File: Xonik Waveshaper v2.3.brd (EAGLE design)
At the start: 55.9 x 21 mm, 78 parts, among them IC1 TL074JT, IC2 TL074JT, IC3 TL074JT, IC4 TL072JT, IC5 4013T, IC6 LM311D, T1 2n3904

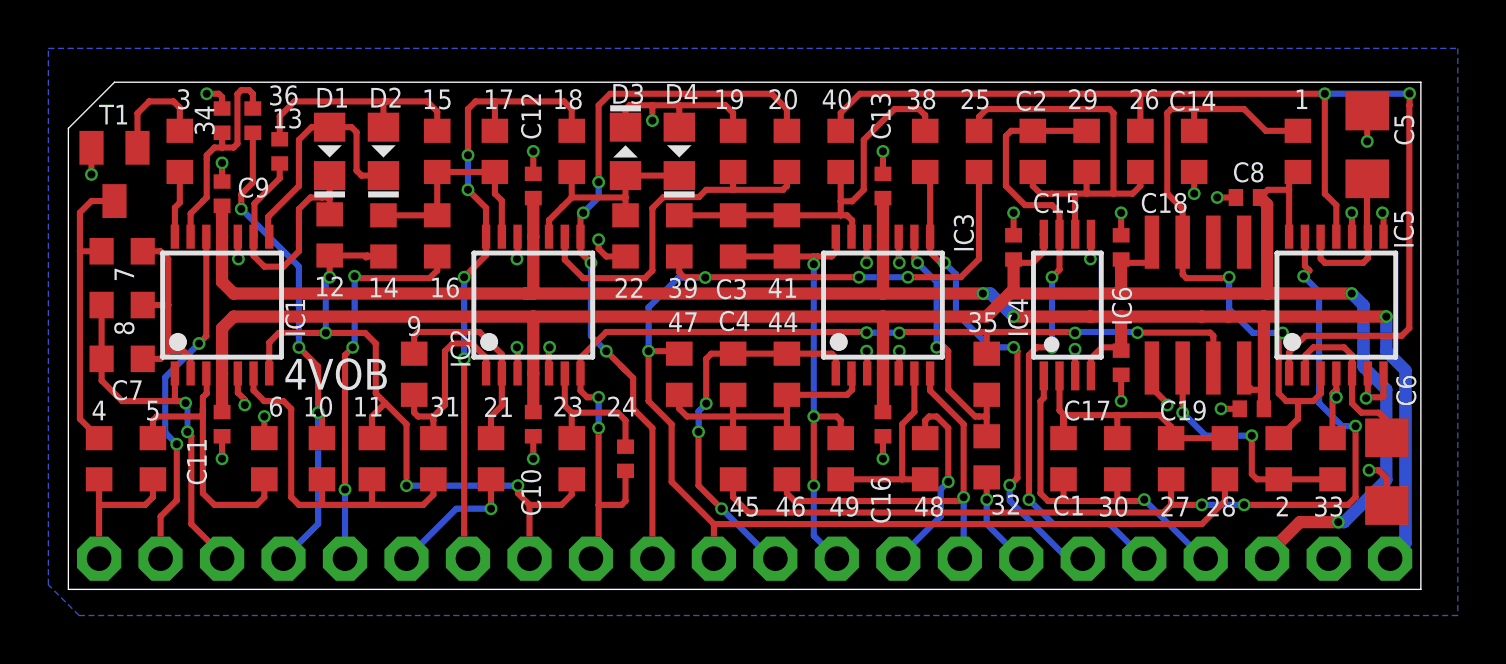
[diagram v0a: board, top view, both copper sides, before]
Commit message: Replaced LM311 with op amp comparator
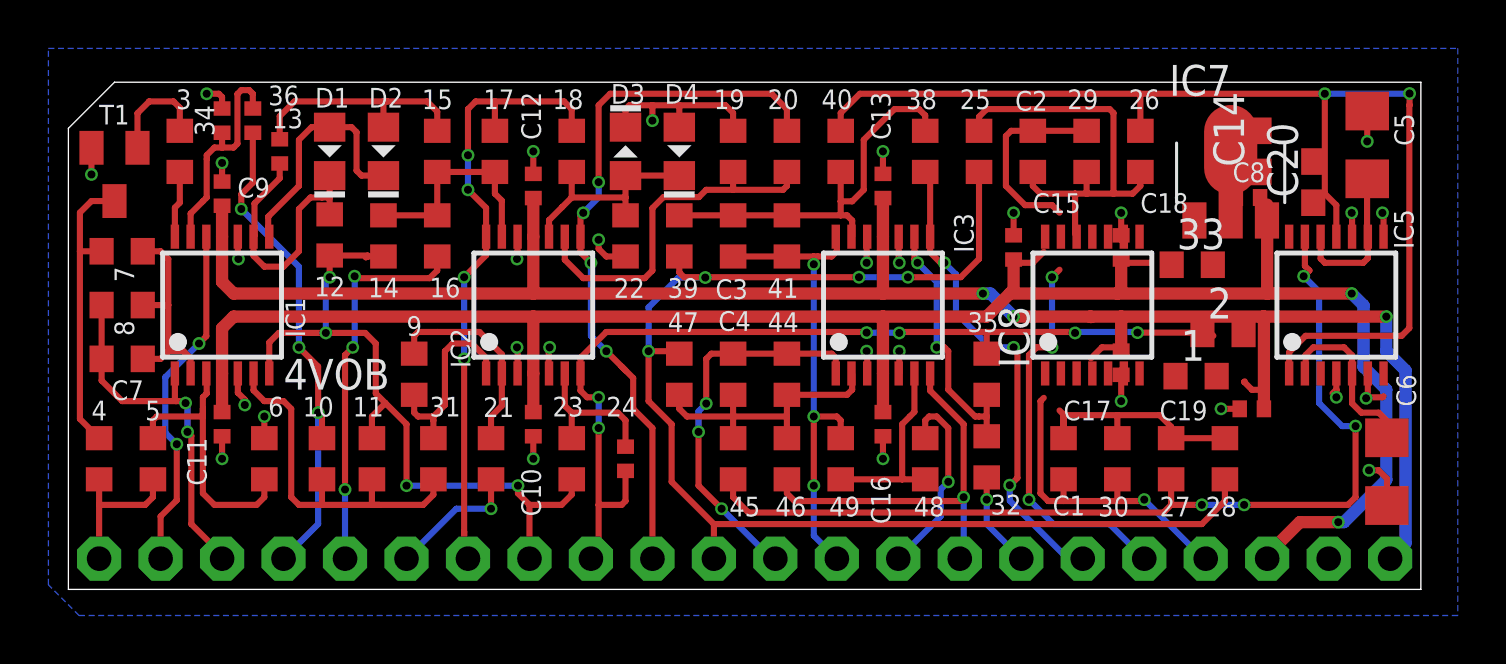
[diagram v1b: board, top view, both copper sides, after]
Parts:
- removed IC4: TL072JT, joakim:TSSOP8J
- removed IC6: LM311D, joakim:SO08J
- added C20: 0.33uF, resistor:C0603
- added IC7: 78L05F, linear:SOT89
- added IC8: TL074JT, joakim:TSSOP14J
- 1: value 510R -> 100k
- 26, 27: value 24k -> 10k
- 33: value 1k -> 20k
- 40, 45: value 120k -> 50k
- C14: value 820pF -> 0.1uF; device joakim:C0603-J -> resistor:C0603
- moved 1 10.2 mm to (46.6, 8.81), turned to 0 degrees
- moved 33 9.89 mm to (46.4, 13.4), turned to 0 degrees
- moved 2 5.65 mm to (47.7, 10.6), turned to 0 degrees
- moved C14 2.70 mm to (49.2, 18.1)
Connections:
- removed net N$25: 2.2, 33.1, IC6.2
- removed net SQR: 1.1, 2.1, C14.2, IC5.3, IC6.7
- new net +5V: C14.2, C8.2, IC5.14, IC7.1
- new net N$17: 33.2, IC5.3, IC8.8
- new net N$7: 1.1, IC8.7
- new net N$9: 1.2, 2.2, 33.1, IC8.9
- net +12V: now also C20.2, IC7.3, IC8.4; no longer 1.2, C8.2, IC4.8, IC5.14, IC6.8
- net -12V: now also 2.1, IC8.11; no longer IC4.4, IC6.4
- net GND: now also C20.1, IC7.2, IC7.2@1, IC8.10, IC8.12, IC8.3, IC8.6; no longer 33.2, IC4.3, IC4.5, IC6.1
- net N$19: now also IC8.13; no longer IC4.6
- net N$22: now also IC8.2; no longer IC4.2
- net SAW: now also IC8.5; no longer IC6.3
- net SUB_SQR_1: now also IC8.14; no longer IC4.7
- net SUB_SQR_2: now also IC8.1; no longer IC4.1
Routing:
- net SQR: track 27.1 -> 0.00 mm, vias 2 -> 0
- net N$25: track 10.2 -> 0.00 mm, vias 2 -> 0
- net GND: track 48.0 -> 39.6 mm, vias 35 -> 30
- net +12V: track 89.1 -> 82.8 mm
- net SUB_SQR_1: track 26.7 -> 24.4 mm
- net -12V: track 81.2 -> 79.5 mm
- net N$22: track 12.0 -> 10.5 mm
- net SAW: track 40.4 -> 39.1 mm
- net SUB_SQR_2: track 15.0 -> 13.9 mm

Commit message: Routed new version of comparator
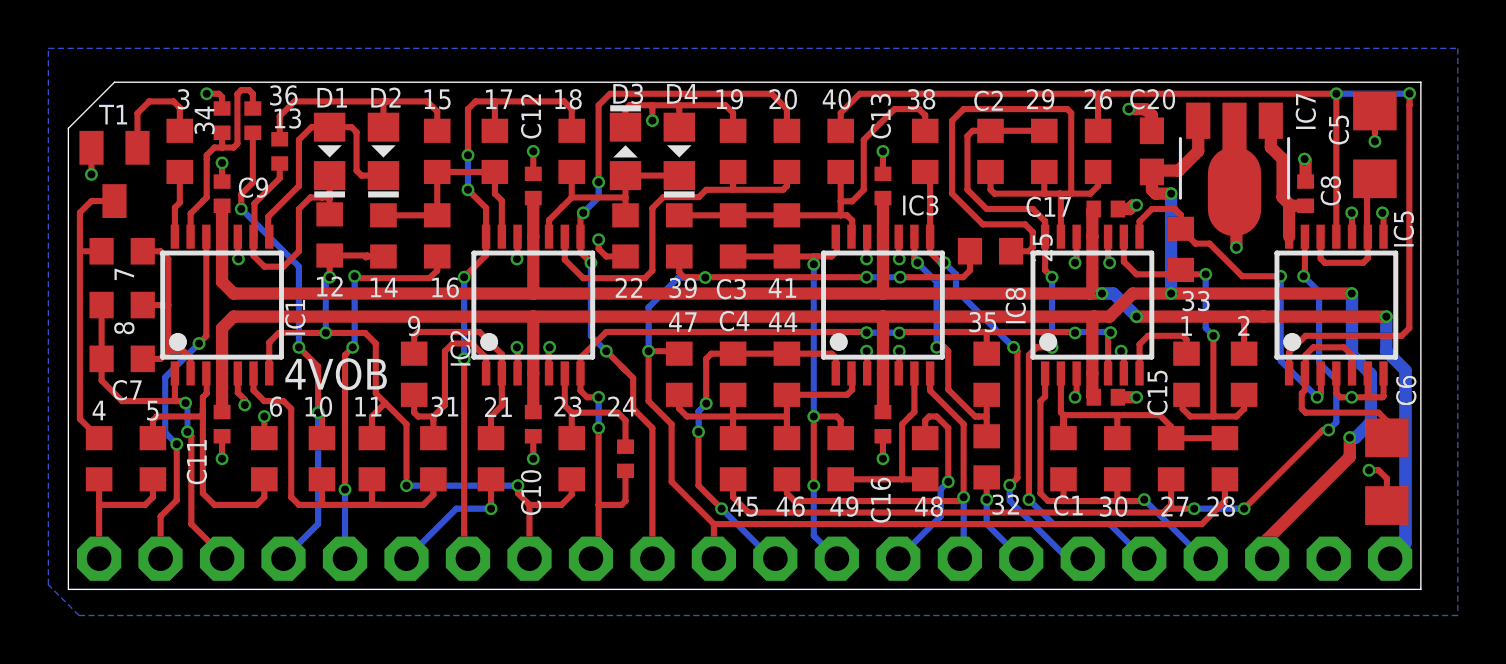
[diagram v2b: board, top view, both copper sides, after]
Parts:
- removed C14: 0.1uF, resistor:C0603
- removed C18, C19: 1uF, joakim:C0402-J
- moved C15 7.27 mm to (42.9, 7.94), turned to 180 degrees
- moved C20 6.79 mm to (44.8, 18.1), turned to 270 degrees
- moved C17 6.38 mm to (42.9, 15.7), turned to 0 degrees
- moved 25 4.15 mm to (38.1, 14.0), turned to 0 degrees
- moved C8 2.39 mm to (51.1, 16.4), turned to 270 degrees
- moved 2 1.88 mm to (48.6, 8.89), turned to 270 degrees
- moved 29 1.75 mm to (40.3, 18.1)
- moved 26 1.75 mm to (42.5, 18.1)
- moved C2 1.75 mm to (38.1, 18.1)
- moved 33 0.79 mm to (46.0, 14.0), turned to 90 degrees
- moved 1 0.40 mm to (46.2, 8.89), turned to 270 degrees
- moved C5 0.32 mm to (54.0, 18.4)
- moved IC7 0.22 mm to (48.2, 17.4), turned to 180 degrees
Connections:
- net +12V: no longer C18.2
- net +5V: no longer C14.2
- net -12V: no longer C19.1
- net GND: no longer C14.1, C18.1, C19.2
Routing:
- net N$9: track 0.00 -> 15.0 mm, vias 0 -> 2
- net N$17: track 0.00 -> 14.8 mm, vias 0 -> 2
- net GND: track 39.6 -> 50.6 mm, vias 30 -> 34
- net N$19: track 18.1 -> 25.8 mm
- net +5V: track 0.00 -> 5.77 mm
- net -12V: track 79.5 -> 75.5 mm
- net N$7: track 0.00 -> 3.93 mm
- net -5V: track 55.3 -> 52.0 mm
- net N$35: track 40.2 -> 37.0 mm
- net SUB_SQR_1: track 24.4 -> 27.4 mm
- net SAW: track 39.1 -> 36.5 mm
- net N$31: track 7.38 -> 9.64 mm
- net +12V: track 82.8 -> 84.5 mm, vias 2 -> 4
- net N$22: track 10.5 -> 12.1 mm
- net SUB_SQR_2: track 13.9 -> 14.9 mm
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
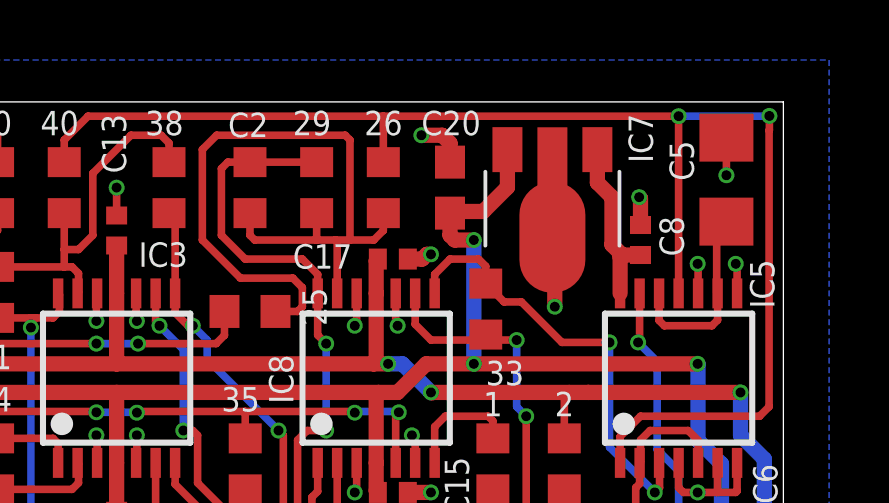
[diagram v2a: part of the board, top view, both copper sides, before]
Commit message: Improved cap footprint
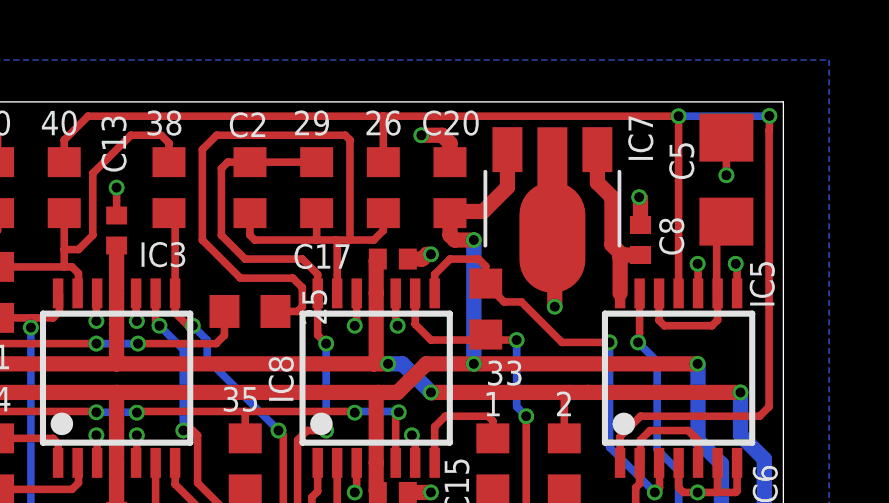
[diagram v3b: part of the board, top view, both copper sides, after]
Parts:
- C20: device resistor:C0603 -> joakim:C0603-J
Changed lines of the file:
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@@
 <attribute name="VALUE" x="50.585725" y="21.728025" size="1.27" layer="27" rot="R180"/>
 </element>
-<element name="C20" library="resistor" package="C0603" value="0.33uF" x="44.7675" y="18.0975" smashed="yes" rot="R270">
+<element name="C20" library="joakim" package="C0603-J" value="0.33uF" x="44.7675" y="18.0975" smashed="yes" rot="R270">
 <attribute name="NAME" x="43.815" y="19.84375" size="0.8128" layer="25" font="vector"/>
 <attribute name="VALUE" x="42.8625" y="18.7325" size="1.27" layer="27" rot="R270"/>

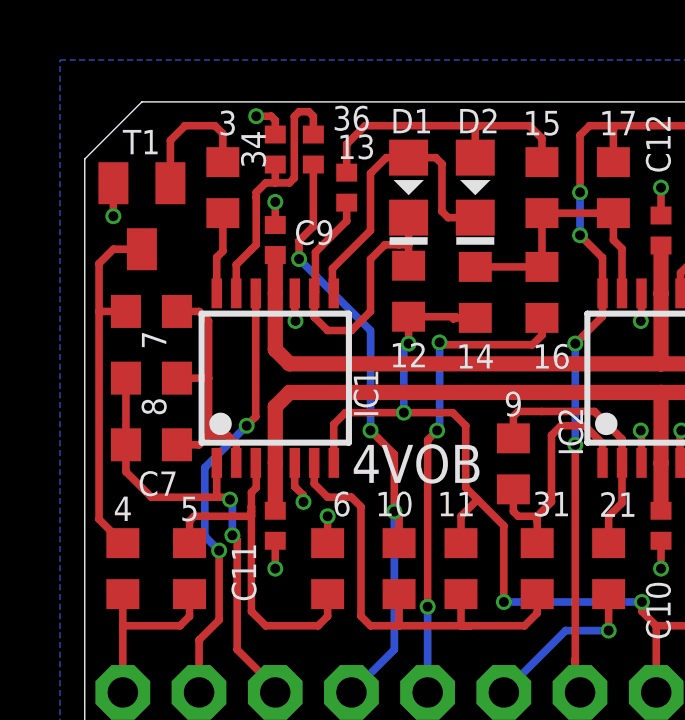
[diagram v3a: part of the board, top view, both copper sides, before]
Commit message: Fixed polarity issue on square wave output
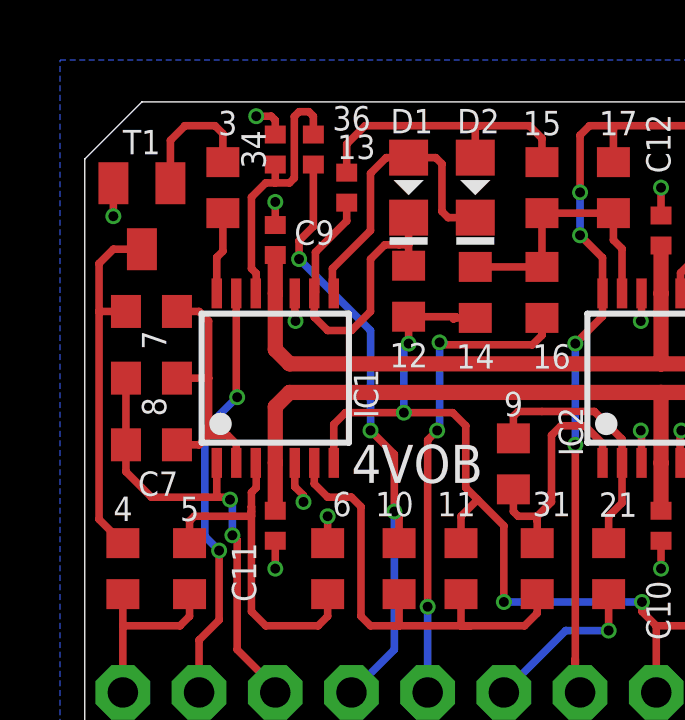
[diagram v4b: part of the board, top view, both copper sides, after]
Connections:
- net N$8: now also IC1.12; no longer IC1.13
- net PW_CV: now also IC1.13; no longer IC1.12
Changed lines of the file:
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@@
 </signal>
 <signal name="PW_CV">
-<contactref element="IC1" pad="12"/>
-<wire x1="5.7" y1="14.5725" x2="5.7" y2="10.4625" width="0.254" layer="1"/>
-<wire x1="5.7" y1="10.4625" x2="5.3975" y2="10.16" width="0.254" layer="1"/>
-<via x="5.3975" y="10.16" extent="1-16" drill="0.3302"/>
+<wire x1="5.05" y1="11.1125" x2="5.08" y2="11.1125" width="0.254" layer="1"/>
+<via x="5.08" y="11.1125" extent="1-16" drill="0.3302"/>
 <wire x1="4.47773125" y1="5.99976875" x2="4.00148125" y2="6.47601875" width="0.254" layer="16"/>
 <via x="4.47773125" y="5.99976875" extent="1-16" drill="0.3302"/>
@@
 <wire x1="3.81" y1="1.27" x2="3.81" y2="3.01625" width="0.254" layer="1"/>
 <wire x1="4.47773125" y1="3.68398125" x2="3.81" y2="3.01625" width="0.254" layer="1"/>
-<wire x1="4.00148125" y1="6.47601875" x2="4.00148125" y2="8.76398125" width="0.254" layer="16"/>
-<wire x1="4.00148125" y1="8.76398125" x2="5.3975" y2="10.16" width="0.254" layer="16"/>
+<wire x1="4.00148125" y1="6.47601875" x2="4.00148125" y2="10.03398125" width="0.254" layer="16"/>
+<wire x1="4.00148125" y1="10.03398125" x2="5.08" y2="11.1125" width="0.254" layer="16"/>
 <contactref element="X1" pad="2"/>
+<contactref element="IC1" pad="13"/>
+<wire x1="5.05" y1="14.5725" x2="5.05" y2="11.1125" width="0.254" layer="1"/>
 </signal>
 <signal name="N$1">
@@
 </signal>
 <signal name="N$8">
-<contactref element="IC1" pad="13"/>
 <contactref element="34" pad="1"/>
 <contactref element="36" pad="2"/>
-<wire x1="5.05" y1="14.5725" x2="5.05" y2="15.5275" width="0.254" layer="1"/>
-<wire x1="5.05" y1="15.5275" x2="5.55625" y2="16.03375" width="0.254" layer="1"/>
-<wire x1="5.55625" y1="16.03375" x2="5.715" y2="16.1925" width="0.254" layer="1"/>
-<wire x1="5.715" y1="16.1925" x2="5.715" y2="17.78" width="0.254" layer="1"/>
-<wire x1="5.715" y1="17.78" x2="5.715" y2="17.93875" width="0.254" layer="1"/>
-<wire x1="5.715" y1="17.93875" x2="6.0325" y2="18.25625" width="0.254" layer="1"/>
+<wire x1="5.55625" y1="15.39875" x2="5.55625" y2="17.78" width="0.254" layer="1"/>
+<wire x1="5.55625" y1="17.78" x2="6.0325" y2="18.25625" width="0.254" layer="1"/>
 <wire x1="6.0325" y1="18.25625" x2="6.35" y2="18.25625" width="0.254" layer="1"/>
 <wire x1="6.35" y1="18.25625" x2="6.82625" y2="18.25625" width="0.254" layer="1"/>
@@
 <wire x1="6.985" y1="18.415" x2="6.985" y2="20.46925" width="0.254" layer="1"/>
 <wire x1="6.35" y1="18.8675" x2="6.35" y2="18.25625" width="0.254" layer="1"/>
+<contactref element="IC1" pad="12"/>
+<wire x1="5.55625" y1="15.39875" x2="5.715" y2="15.24" width="0.254" layer="1"/>
+<wire x1="5.715" y1="15.24" x2="5.715" y2="14.5875" width="0.254" layer="1"/>
+<wire x1="5.715" y1="14.5875" x2="5.7" y2="14.5725" width="0.254" layer="1"/>
 </signal>
 <signal name="N$9">
